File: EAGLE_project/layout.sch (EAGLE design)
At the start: 15 parts

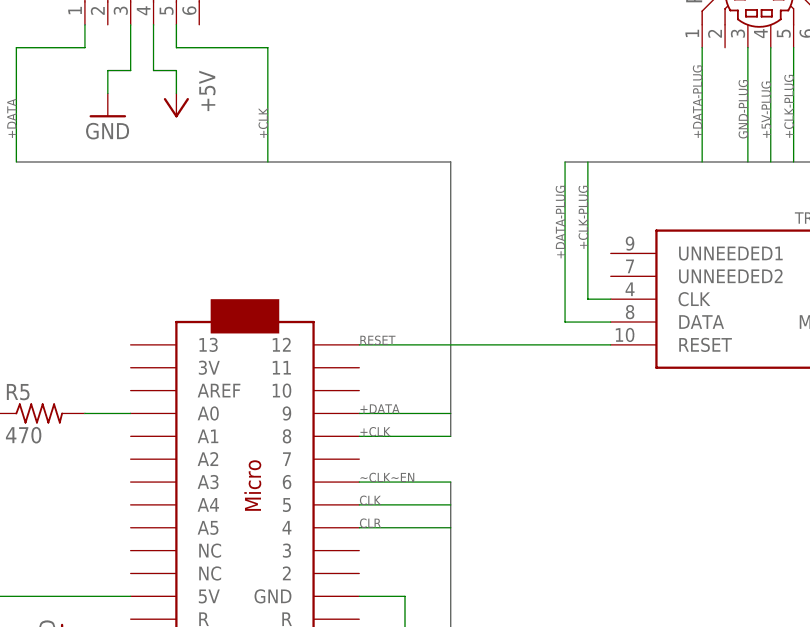
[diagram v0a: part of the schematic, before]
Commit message: Change TrackPoint CLK from Arduino pin 8 to 7
This is to have it on an interrupt, necessary for stream mode.
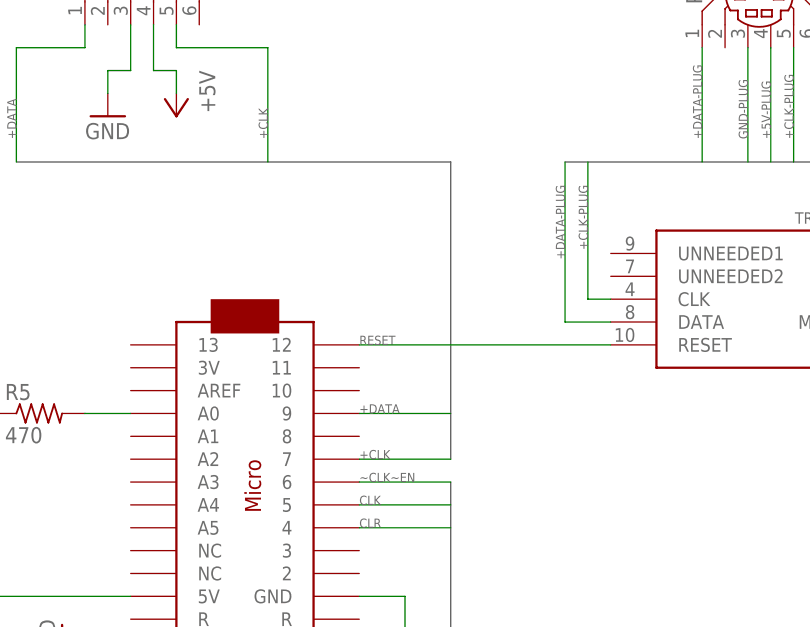
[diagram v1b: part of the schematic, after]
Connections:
- net +CLK: now also U$2.7; no longer U$2.8
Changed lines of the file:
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@@
 <bus name="+DATA,+CLK">
 <segment>
-<wire x1="-2.54" y1="48.26" x2="-2.54" y2="78.74" width="0.762" layer="92"/>
+<wire x1="-2.54" y1="45.72" x2="-2.54" y2="78.74" width="0.762" layer="92"/>
 <wire x1="-50.8" y1="78.74" x2="-2.54" y2="78.74" width="0.762" layer="92"/>
 </segment>
@@
 <net name="+CLK" class="0">
 <segment>
-<pinref part="U$2" gate="G$1" pin="8"/>
-<wire x1="-2.54" y1="48.26" x2="-12.7" y2="48.26" width="0.1524" layer="91"/>
-<label x="-12.7" y="48.26" size="1.016" layer="95"/>
-</segment>
-<segment>
 <wire x1="-33.02" y1="91.44" x2="-22.86" y2="91.44" width="0.1524" layer="91"/>
 <pinref part="PS/2" gate="G$1" pin="5"/>
@@
 <label x="-22.86" y="81.28" size="1.016" layer="95" rot="R90"/>
 </segment>
-</net>
+<segment>
+<pinref part="U$2" gate="G$1" pin="7"/>
+<wire x1="-12.7" y1="45.72" x2="-2.54" y2="45.72" width="0.1524" layer="91"/>
+<label x="-12.7" y="45.72" size="1.016" layer="95"/>
+</segment>
+</net>

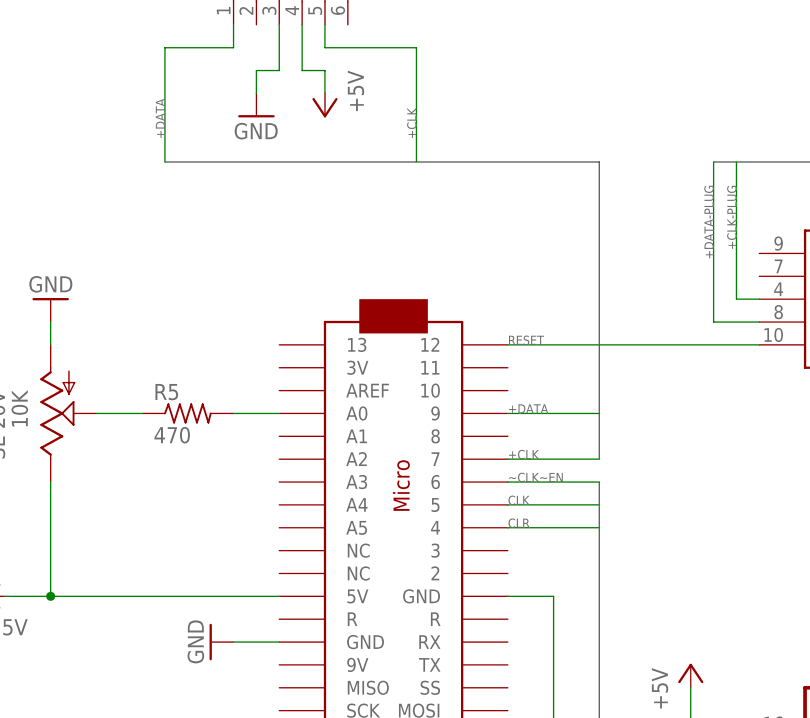
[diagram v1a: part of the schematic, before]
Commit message: Change TrackPoint CLK from Arduino pin 7 to 3
With pin 7, when lifting the finger from the TrackPoint, then cursor movement
doesn't stop. This happens with the following library and the issue is
confirmed by its author.

https://github.com/rampadc/arduino-trackpoint-extended
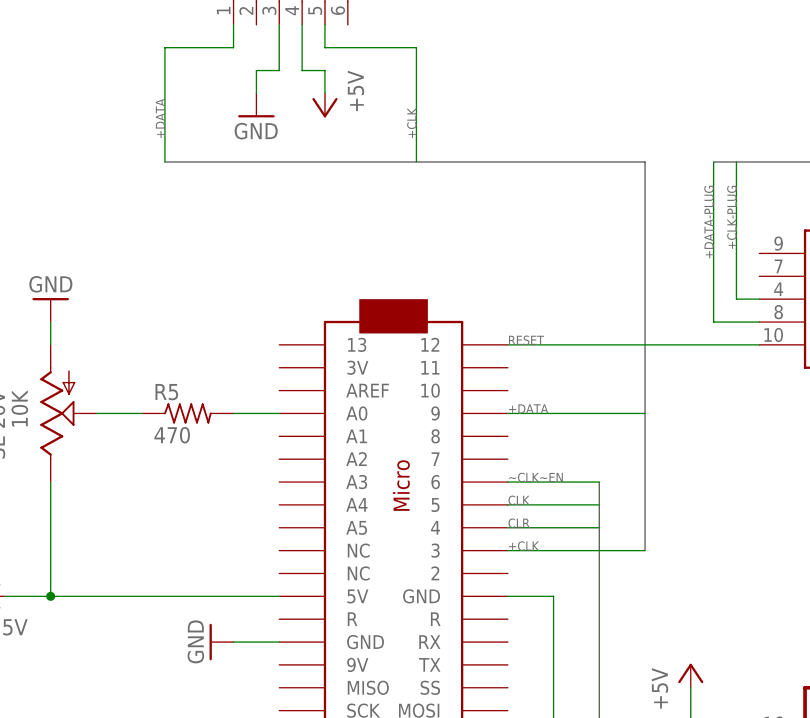
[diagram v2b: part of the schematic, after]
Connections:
- net +CLK: now also U$2.3; no longer U$2.7
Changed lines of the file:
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@@
 <bus name="+DATA,+CLK">
 <segment>
-<wire x1="-2.54" y1="45.72" x2="-2.54" y2="78.74" width="0.762" layer="92"/>
-<wire x1="-50.8" y1="78.74" x2="-2.54" y2="78.74" width="0.762" layer="92"/>
+<wire x1="2.54" y1="35.56" x2="2.54" y2="78.74" width="0.762" layer="92"/>
+<wire x1="-50.8" y1="78.74" x2="2.54" y2="78.74" width="0.762" layer="92"/>
 </segment>
 </bus>
@@
 </segment>
 <segment>
-<pinref part="U$2" gate="G$1" pin="7"/>
-<wire x1="-12.7" y1="45.72" x2="-2.54" y2="45.72" width="0.1524" layer="91"/>
-<label x="-12.7" y="45.72" size="1.016" layer="95"/>
+<pinref part="U$2" gate="G$1" pin="3"/>
+<wire x1="-12.7" y1="35.56" x2="2.54" y2="35.56" width="0.1524" layer="91"/>
+<label x="-12.7" y="35.56" size="1.016" layer="95"/>
 </segment>
 </net>
@@
 <segment>
 <pinref part="U$2" gate="G$1" pin="9"/>
-<wire x1="-2.54" y1="50.8" x2="-12.7" y2="50.8" width="0.1524" layer="91"/>
+<wire x1="2.54" y1="50.8" x2="-12.7" y2="50.8" width="0.1524" layer="91"/>
 <label x="-12.7" y="50.8" size="1.016" layer="95"/>
 </segment>
